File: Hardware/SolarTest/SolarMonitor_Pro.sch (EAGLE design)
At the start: 34 parts, among them J6 5.5x2.1mm Barrel, J8 CONN_42.54_SCREW, U1 INA219DCN, U2 INA219DCN, U3 INA219DCN

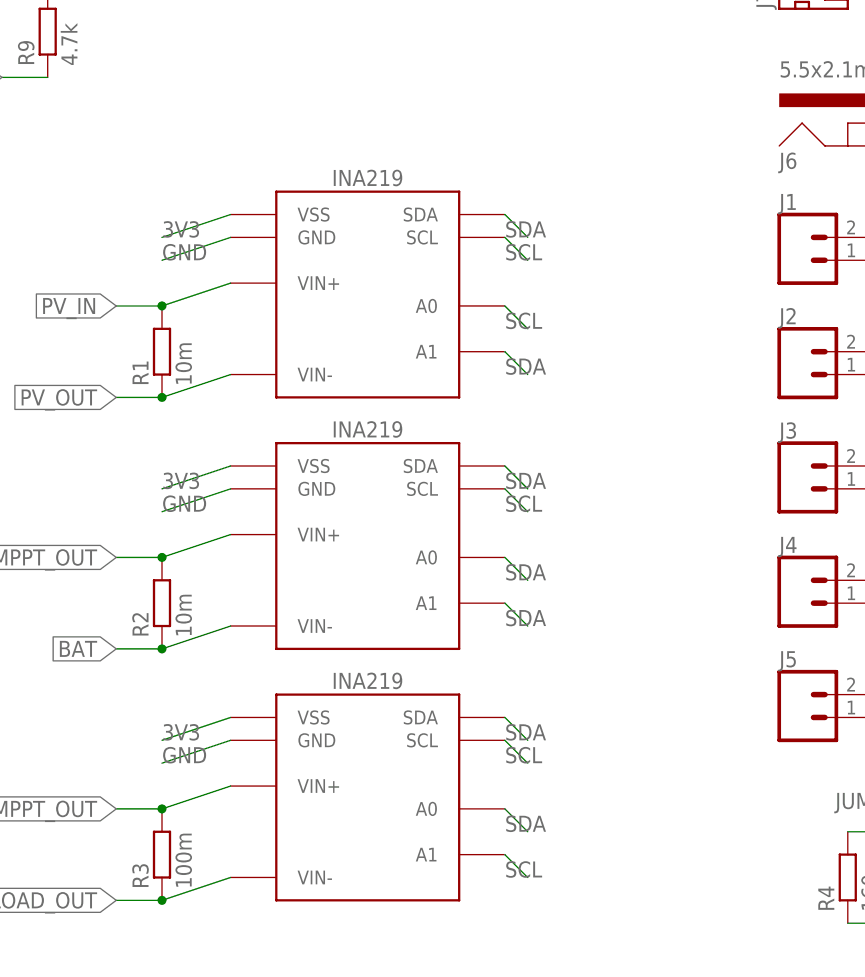
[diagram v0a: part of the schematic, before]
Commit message: Added BOM, added ADR info to schematic
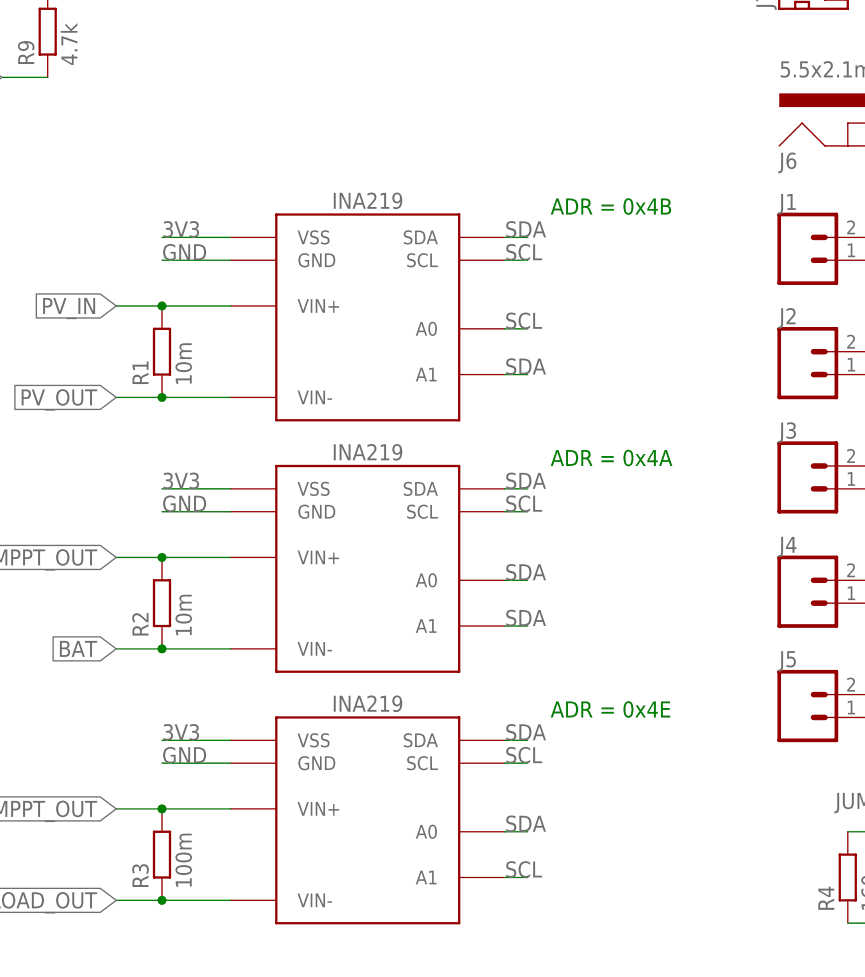
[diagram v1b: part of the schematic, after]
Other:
- note added: "ADR = 0x4A"
- note added: "ADR = 0x4B"
- note added: "ADR = 0x4E"
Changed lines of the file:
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@@
 <sheet>
 <plain>
+<text x="190.5" y="93.98" size="1.778" layer="91">ADR = 0x4B</text>
+<text x="190.5" y="66.04" size="1.778" layer="91">ADR = 0x4A</text>
+<text x="190.5" y="38.1" size="1.778" layer="91">ADR = 0x4E</text>
 </plain>
 <instances>
-<instance part="U1" gate="G$1" x="170.18" y="83.82" smashed="yes"/>
+<instance part="U1" gate="G$1" x="170.18" y="81.28" smashed="yes"/>
 <instance part="R1" gate="G$1" x="147.32" y="78.74" smashed="yes" rot="R90">
 <attribute name="NAME" x="145.8214" y="74.93" size="1.778" layer="95" rot="R90"/>
@@
 <attribute name="NAME" x="215.9" y="43.688" size="1.778" layer="95" font="vector"/>
 </instance>
-<instance part="U2" gate="G$1" x="170.18" y="55.88" smashed="yes"/>
+<instance part="U2" gate="G$1" x="170.18" y="53.34" smashed="yes"/>
 <instance part="R2" gate="G$1" x="147.32" y="50.8" smashed="yes" rot="R90">
 <attribute name="NAME" x="145.8214" y="46.99" size="1.778" layer="95" rot="R90"/>
 <attribute name="VALUE" x="150.622" y="46.99" size="1.778" layer="96" rot="R90"/>
 </instance>
-<instance part="U3" gate="G$1" x="170.18" y="27.94" smashed="yes"/>
+<instance part="U3" gate="G$1" x="170.18" y="25.4" smashed="yes"/>
 <instance part="R3" gate="G$1" x="147.32" y="22.86" smashed="yes" rot="R90">
 <attribute name="NAME" x="145.8214" y="19.05" size="1.778" layer="95" rot="R90"/>
@@
 <segment>
 <pinref part="U1" gate="G$1" pin="SCL"/>
-<wire x1="185.42" y1="91.44" x2="187.96" y2="88.9" width="0.1524" layer="91"/>
+<wire x1="185.42" y1="88.9" x2="187.96" y2="88.9" width="0.1524" layer="91"/>
 <label x="185.42" y="88.9" size="1.778" layer="95"/>
 </segment>
 <segment>
 <pinref part="U2" gate="G$1" pin="SCL"/>
-<wire x1="185.42" y1="63.5" x2="187.96" y2="60.96" width="0.1524" layer="91"/>
+<wire x1="185.42" y1="60.96" x2="187.96" y2="60.96" width="0.1524" layer="91"/>
 <label x="185.42" y="60.96" size="1.778" layer="95"/>
 </segment>
 <segment>
 <pinref part="U3" gate="G$1" pin="SCL"/>
-<wire x1="185.42" y1="35.56" x2="187.96" y2="33.02" width="0.1524" layer="91"/>
+<wire x1="185.42" y1="33.02" x2="187.96" y2="33.02" width="0.1524" layer="91"/>
 <label x="185.42" y="33.02" size="1.778" layer="95"/>
 </segment>
 <segment>
 <pinref part="U3" gate="G$1" pin="A1"/>
-<wire x1="187.96" y1="20.32" x2="185.42" y2="22.86" width="0.1524" layer="91"/>
+<wire x1="187.96" y1="20.32" x2="185.42" y2="20.32" width="0.1524" layer="91"/>
 <label x="185.42" y="20.32" size="1.778" layer="95"/>
 </segment>
@@
 <segment>
 <pinref part="U1" gate="G$1" pin="A0"/>
-<wire x1="185.42" y1="83.82" x2="187.96" y2="81.28" width="0.1524" layer="91"/>
+<wire x1="185.42" y1="81.28" x2="187.96" y2="81.28" width="0.1524" layer="91"/>
 <label x="185.42" y="81.28" size="1.778" layer="95"/>
 </segment>
@@
 <segment>
 <pinref part="U1" gate="G$1" pin="SDA"/>
-<wire x1="185.42" y1="93.98" x2="187.96" y2="91.44" width="0.1524" layer="91"/>
+<wire x1="185.42" y1="91.44" x2="187.96" y2="91.44" width="0.1524" layer="91"/>
 <label x="185.42" y="91.44" size="1.778" layer="95"/>
 </segment>
 <segment>
 <pinref part="U2" gate="G$1" pin="SDA"/>
-<wire x1="185.42" y1="66.04" x2="187.96" y2="63.5" width="0.1524" layer="91"/>
+<wire x1="185.42" y1="63.5" x2="187.96" y2="63.5" width="0.1524" layer="91"/>
 <label x="185.42" y="63.5" size="1.778" layer="95"/>
 </segment>
 <segment>
 <pinref part="U3" gate="G$1" pin="SDA"/>
-<wire x1="185.42" y1="38.1" x2="187.96" y2="35.56" width="0.1524" layer="91"/>
+<wire x1="185.42" y1="35.56" x2="187.96" y2="35.56" width="0.1524" layer="91"/>
 <label x="185.42" y="35.56" size="1.778" layer="95"/>
 </segment>
 <segment>
 <pinref part="U3" gate="G$1" pin="A0"/>
-<wire x1="185.42" y1="27.94" x2="187.96" y2="25.4" width="0.1524" layer="91"/>
+<wire x1="185.42" y1="25.4" x2="187.96" y2="25.4" width="0.1524" layer="91"/>
 <label x="185.42" y="25.4" size="1.778" layer="95"/>
 </segment>
 <segment>
 <pinref part="U2" gate="G$1" pin="A0"/>
-<wire x1="185.42" y1="55.88" x2="187.96" y2="53.34" width="0.1524" layer="91"/>
+<wire x1="185.42" y1="53.34" x2="187.96" y2="53.34" width="0.1524" layer="91"/>
 <label x="185.42" y="53.34" size="1.778" layer="95"/>
 </segment>
 <segment>
 <pinref part="U2" gate="G$1" pin="A1"/>
-<wire x1="187.96" y1="48.26" x2="185.42" y2="50.8" width="0.1524" layer="91"/>
+<wire x1="187.96" y1="48.26" x2="185.42" y2="48.26" width="0.1524" layer="91"/>
 <label x="185.42" y="48.26" size="1.778" layer="95"/>
 </segment>
@@
 <segment>
 <pinref part="U1" gate="G$1" pin="A1"/>
-<wire x1="187.96" y1="76.2" x2="185.42" y2="78.74" width="0.1524" layer="91"/>
+<wire x1="187.96" y1="76.2" x2="185.42" y2="76.2" width="0.1524" layer="91"/>
 <label x="185.42" y="76.2" size="1.778" layer="95"/>
 </segment>
@@
 <segment>
 <pinref part="U1" gate="G$1" pin="VSS"/>
-<wire x1="154.94" y1="93.98" x2="147.32" y2="91.44" width="0.1524" layer="91"/>
+<wire x1="154.94" y1="91.44" x2="147.32" y2="91.44" width="0.1524" layer="91"/>
 <label x="147.32" y="91.44" size="1.778" layer="95"/>
 </segment>
 <segment>
 <pinref part="U2" gate="G$1" pin="VSS"/>
-<wire x1="154.94" y1="66.04" x2="147.32" y2="63.5" width="0.1524" layer="91"/>
+<wire x1="154.94" y1="63.5" x2="147.32" y2="63.5" width="0.1524" layer="91"/>
 <label x="147.32" y="63.5" size="1.778" layer="95"/>
 </segment>
 <segment>
 <pinref part="U3" gate="G$1" pin="VSS"/>
-<wire x1="154.94" y1="38.1" x2="147.32" y2="35.56" width="0.1524" layer="91"/>
+<wire x1="154.94" y1="35.56" x2="147.32" y2="35.56" width="0.1524" layer="91"/>
 <label x="147.32" y="35.56" size="1.778" layer="95"/>
 </segment>
@@
 <segment>
 <pinref part="U1" gate="G$1" pin="GND"/>
-<wire x1="154.94" y1="91.44" x2="147.32" y2="88.9" width="0.1524" layer="91"/>
+<wire x1="154.94" y1="88.9" x2="147.32" y2="88.9" width="0.1524" layer="91"/>
 <label x="147.32" y="88.9" size="1.778" layer="95"/>
 </segment>
@@
 <segment>
 <pinref part="U2" gate="G$1" pin="GND"/>
-<wire x1="154.94" y1="63.5" x2="147.32" y2="60.96" width="0.1524" layer="91"/>
+<wire x1="154.94" y1="60.96" x2="147.32" y2="60.96" width="0.1524" layer="91"/>
 <label x="147.32" y="60.96" size="1.778" layer="95"/>
 </segment>
 <segment>
 <pinref part="U3" gate="G$1" pin="GND"/>
-<wire x1="154.94" y1="35.56" x2="147.32" y2="33.02" width="0.1524" layer="91"/>
+<wire x1="154.94" y1="33.02" x2="147.32" y2="33.02" width="0.1524" layer="91"/>
 <label x="147.32" y="33.02" size="1.778" layer="95"/>
 </segment>
@@
 <pinref part="U1" gate="G$1" pin="VIN+"/>
 <pinref part="R1" gate="G$1" pin="2"/>
-<wire x1="154.94" y1="86.36" x2="147.32" y2="83.82" width="0.1524" layer="91"/>
+<wire x1="154.94" y1="83.82" x2="147.32" y2="83.82" width="0.1524" layer="91"/>
 <wire x1="147.32" y1="83.82" x2="142.24" y2="83.82" width="0.1524" layer="91"/>
 <junction x="147.32" y="83.82"/>
@@
 <pinref part="U1" gate="G$1" pin="VIN-"/>
 <pinref part="R1" gate="G$1" pin="1"/>
-<wire x1="154.94" y1="76.2" x2="147.32" y2="73.66" width="0.1524" layer="91"/>
+<wire x1="154.94" y1="73.66" x2="147.32" y2="73.66" width="0.1524" layer="91"/>
 <wire x1="147.32" y1="73.66" x2="142.24" y2="73.66" width="0.1524" layer="91"/>
 <junction x="147.32" y="73.66"/>
@@
 <pinref part="U2" gate="G$1" pin="VIN-"/>
 <pinref part="R2" gate="G$1" pin="1"/>
-<wire x1="154.94" y1="48.26" x2="147.32" y2="45.72" width="0.1524" layer="91"/>
+<wire x1="154.94" y1="45.72" x2="147.32" y2="45.72" width="0.1524" layer="91"/>
 <wire x1="147.32" y1="45.72" x2="142.24" y2="45.72" width="0.1524" layer="91"/>
 <junction x="147.32" y="45.72"/>
@@
 <pinref part="U2" gate="G$1" pin="VIN+"/>
 <pinref part="R2" gate="G$1" pin="2"/>
-<wire x1="154.94" y1="58.42" x2="147.32" y2="55.88" width="0.1524" layer="91"/>
+<wire x1="154.94" y1="55.88" x2="147.32" y2="55.88" width="0.1524" layer="91"/>
 <wire x1="147.32" y1="55.88" x2="142.24" y2="55.88" width="0.1524" layer="91"/>
 <junction x="147.32" y="55.88"/>
@@
 <pinref part="U3" gate="G$1" pin="VIN+"/>
 <pinref part="R3" gate="G$1" pin="2"/>
-<wire x1="154.94" y1="30.48" x2="147.32" y2="27.94" width="0.1524" layer="91"/>
+<wire x1="154.94" y1="27.94" x2="147.32" y2="27.94" width="0.1524" layer="91"/>
 <wire x1="147.32" y1="27.94" x2="142.24" y2="27.94" width="0.1524" layer="91"/>
 <junction x="147.32" y="27.94"/>
@@
 <pinref part="U3" gate="G$1" pin="VIN-"/>
 <pinref part="R3" gate="G$1" pin="1"/>
-<wire x1="154.94" y1="20.32" x2="147.32" y2="17.78" width="0.1524" layer="91"/>
+<wire x1="154.94" y1="17.78" x2="147.32" y2="17.78" width="0.1524" layer="91"/>
 <wire x1="147.32" y1="17.78" x2="142.24" y2="17.78" width="0.1524" layer="91"/>
 <junction x="147.32" y="17.78"/>
